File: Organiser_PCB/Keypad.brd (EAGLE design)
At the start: 70.2 x 107 mm, 54 parts, among them IC1 MCP23017SO

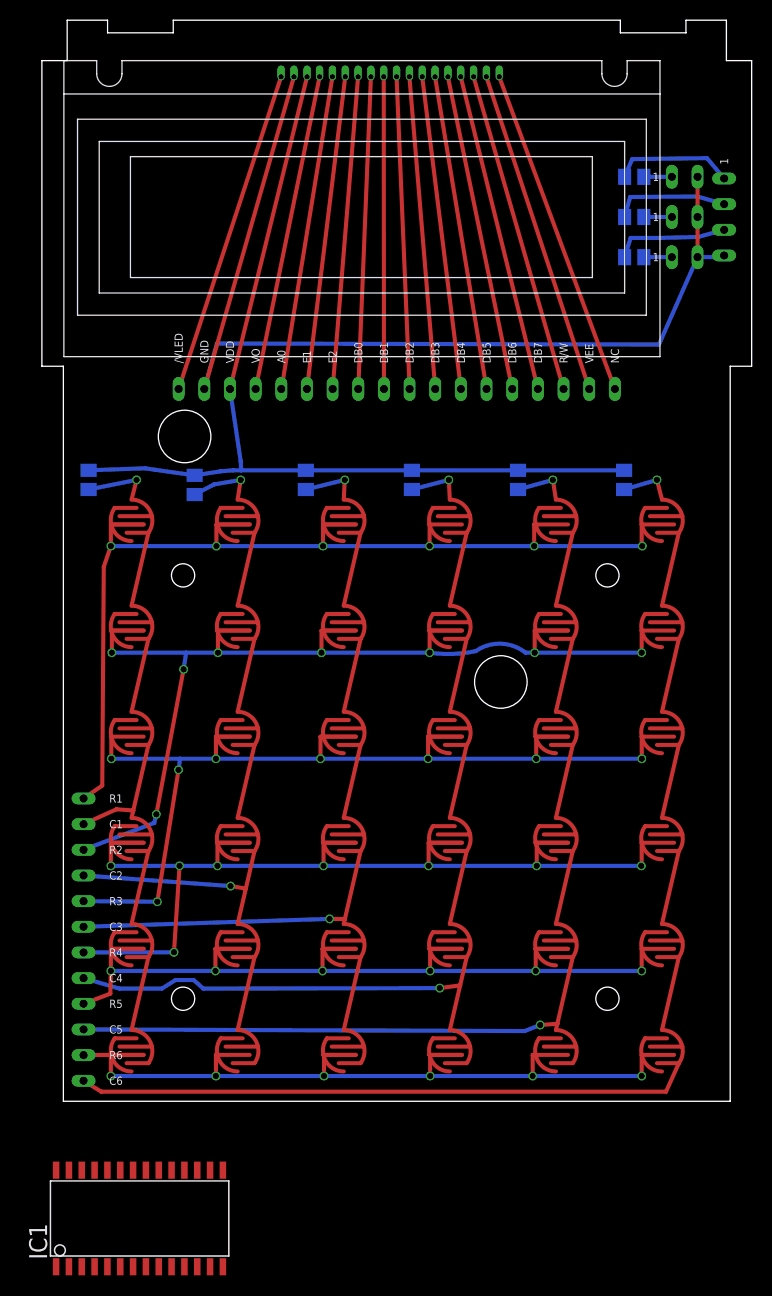
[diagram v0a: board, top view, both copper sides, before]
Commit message: Changed LCD to use MCP23S17 with SPI interface Reduced example execution time to draw on LCD from 4 seconds down to 251 ms (I2C to SPI)
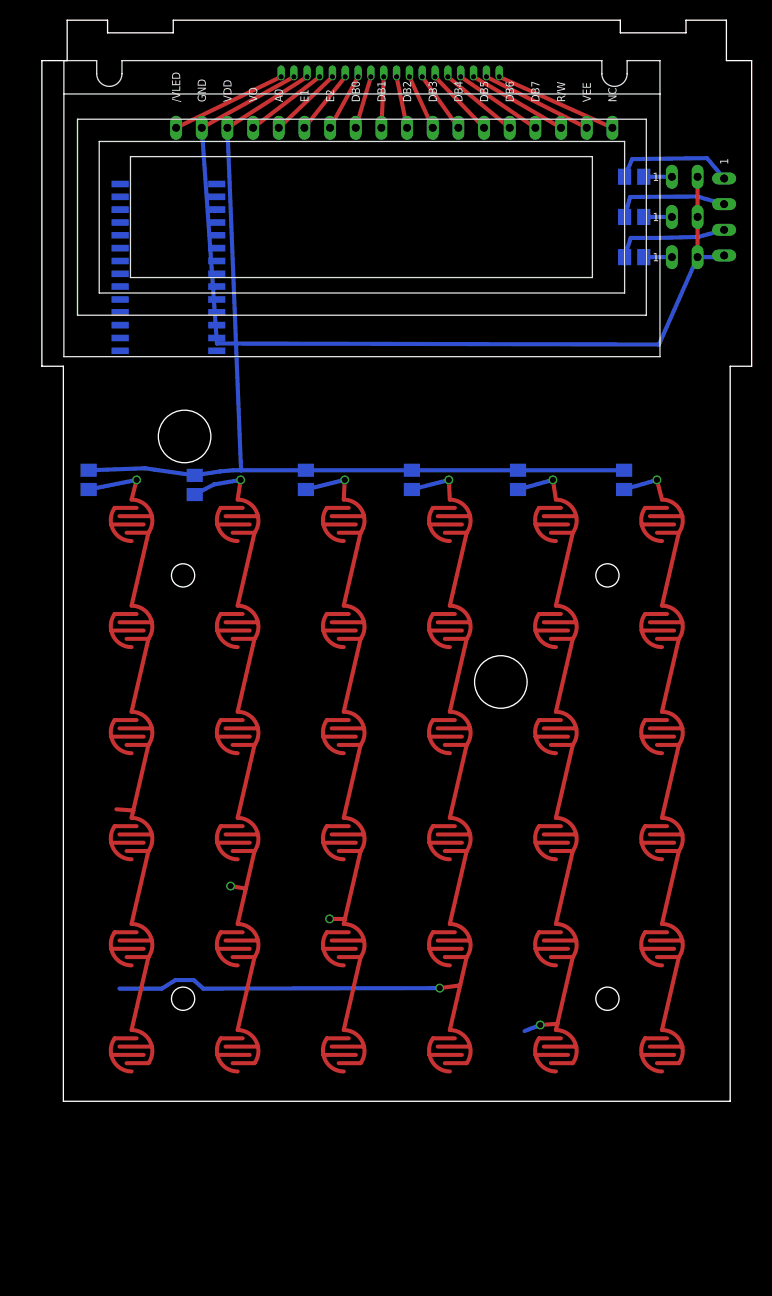
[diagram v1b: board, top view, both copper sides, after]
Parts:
- removed U$37: HEADER-1X12-KEYPAD, teelsys-0.2:HEADER-1X12-KEYPAD
- moved IC1 93.6 mm to (10.4, 81.9), flipped to the bottom, turned to 90 degrees
- moved U$38 25.9 mm to (32.8, 96.3)
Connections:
- net COL_1: no longer U$37.COL_1
- net COL_2: no longer U$37.COL_2
- net COL_3: no longer U$37.COL_3
- net COL_4: no longer U$37.COL_4
- net COL_5: no longer U$37.COL_5
- net COL_6: no longer U$37.COL_6
- net ROW_1: no longer U$37.ROW_1
- net ROW_2: no longer U$37.ROW_2
- net ROW_3: no longer U$37.ROW_3
- net ROW_4: no longer U$37.ROW_4
- net ROW_5: no longer U$37.ROW_5
- net ROW_6: no longer U$37.ROW_6
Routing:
- net ROW_2: track 106.4 -> 0.00 mm, vias 8 -> 0
- net ROW_1: track 101.5 -> 0.00 mm, vias 6 -> 0
- net ROW_3: track 100.6 -> 0.00 mm, vias 8 -> 0
- net ROW_4: track 99.8 -> 0.00 mm, vias 8 -> 0
- net ROW_5: track 87.1 -> 0.00 mm, vias 6 -> 0
- net ROW_6: track 77.8 -> 0.00 mm, vias 6 -> 0
- net COL_6: track 103.5 -> 42.5 mm
- net COL_5: track 89.6 -> 46.0 mm
- net DB1: track 30.9 -> 5.06 mm
- net DB2: track 30.9 -> 5.16 mm
- net DB0: track 30.9 -> 5.27 mm
- net DB3: track 31.0 -> 5.55 mm
- net A0: track 32.4 -> 7.09 mm
- net E2: track 31.0 -> 5.76 mm
- net DB4: track 31.1 -> 6.19 mm
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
